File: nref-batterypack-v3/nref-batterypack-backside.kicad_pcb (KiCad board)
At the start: 2 copper layers, 75 x 17 mm, 8 parts, among them J1 C1+, J2 C2-, J3 C3+, J4 C4-, J5 FRONT_CONN

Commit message: battpack v3 snapshot
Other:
- board text added: "TODO: 4 layers to ensure thickness!"
- board text added: "TODO: fix holes etc"
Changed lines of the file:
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@@
 		(layer "Edge.Cuts")
+	)
+	(gr_text "TODO: fix holes etc"
+		(at 117.2 79.5 0)
+		(layer "Dwgs.User")
+		(effects
+			(font
+				(size 1 1)
+				(thickness 0.15)
+			)
+			(justify left bottom)
+		)
+	)
+	(gr_text "TODO: 4 layers to ensure thickness!"
+		(at 117.4 77.2 0)
+		(layer "Dwgs.User")
+		(effects
+			(font
+				(size 1 1)
+				(thickness 0.15)
+			)
+			(justify left bottom)
+		)
 	)
 	(segment

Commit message: batterypack v3 front+back pcbs polished for ordering
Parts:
- removed H2: MountingHole, MountingHole:MountingHole_2.2mm_M2
- J1, J3: footprint footprints:S713145R -> footprints:S174146R
- J2, J4: footprint footprints:S713145R -> footprints:S70332002045R
- J5: footprint Connector_JST:JST_SHL_SM02B-SHLS-TF_1x02-1MP_P1.00mm_Horizontal -> Connector_JST:JST_SH_SM02B-SRSS-TB_1x02-1MP_P1.00mm_Horizontal
- moved H1 35.0 mm to (127.5, 97.3)
- moved H3 1.10 mm to (127.5, 92.2)
- moved J5 0.35 mm to (127.9, 86.0)
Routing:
- net /C3+: vias 1 -> 5
- net /C1+: vias 1 -> 8
- added copper zone on B.Cu, net /C1+
- added copper zone on In1.Cu, net /C1+
- added copper zone on In2.Cu, net /C1+
- added copper zone on B.Cu, net /C3+
- added copper zone on In1.Cu, net /C3+
- added copper zone on In2.Cu, net /C3+
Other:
- outline, holes or cut-outs redrawn
- copper layers 2 -> 4
- board text added: "+"
- board text added: "–"
- board text removed: "TODO: 4 layers to ensure thickness!"
- board text removed: "TODO: fix holes etc"

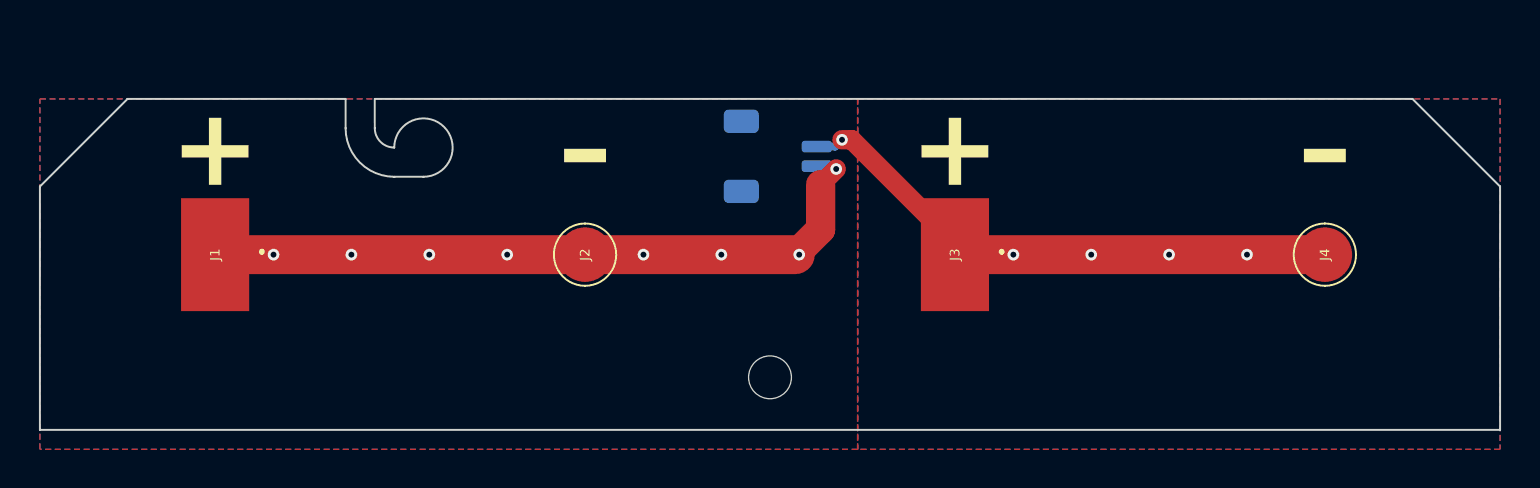
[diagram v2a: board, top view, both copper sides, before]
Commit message: batterypack back/front: polishing for production
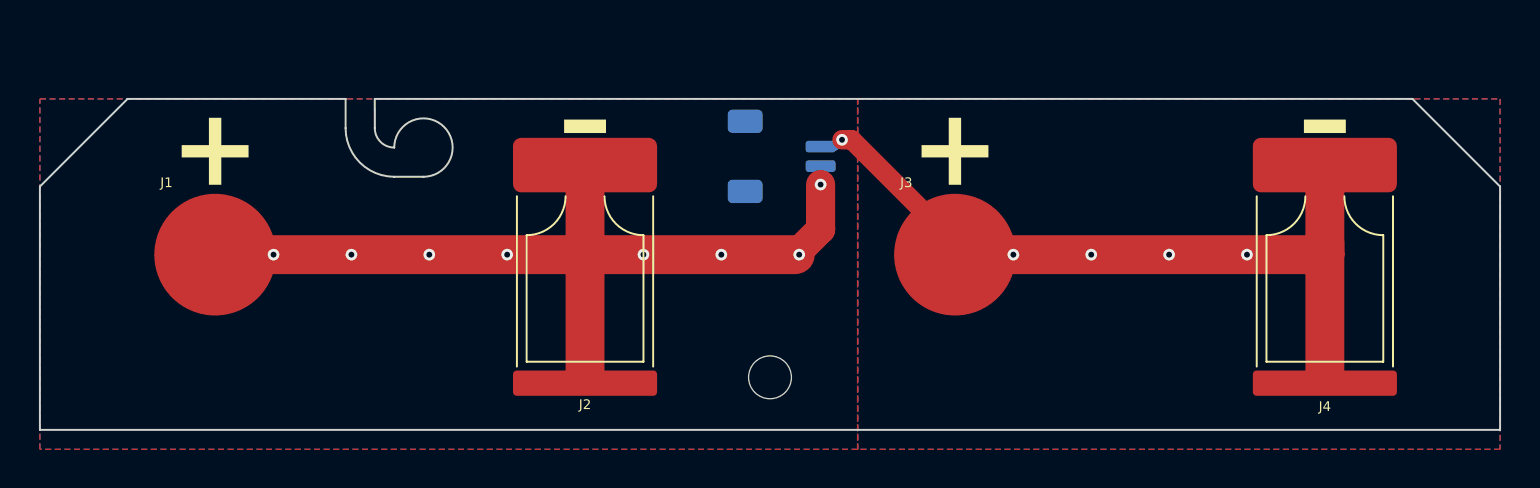
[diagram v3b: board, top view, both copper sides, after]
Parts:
- J1, J3: footprint footprints:S174146R -> footprints:Mill-Max_2036-X-57
- J2, J4: footprint footprints:S70332002045R -> footprints:MYOUNG_MY-FJ-115
- moved H3 28.7 mm to (99.2, 96.9)
- moved J2 1.00 mm to (118.0, 92.0), turned to 180 degrees
- moved J4 1.00 mm to (156.0, 92.0), turned to 180 degrees
- moved J5 0.20 mm to (128.1, 86.0)
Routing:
- net /C3+: track 29.0 -> 40.0 mm
- net /C1+: track 36.1 -> 46.2 mm
